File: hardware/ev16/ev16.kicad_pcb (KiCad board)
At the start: 4 copper layers, 109.8 x 80 mm, 162 parts, among them CN1 Conn_05x02_Female, CN2 PJ-242, J1 USB_C_Receptacle, J11 Conn_02x05_Counter_Clockwise, J2 Conn_01x02_Socket, J3 AudioJack4, J4 Conn_02x03_Odd_Even, J5 Conn_02x03_Odd_Even, J6 Conn_02x05_Counter_Clockwise, J7 Conn_02x05_Counter_Clockwise, J8 Conn_02x05_Counter_Clockwise, J9 Conn_02x05_Counter_Clockwise, Q1 2N7002, SW1 SW_SPDT, SW2 SW_Push, SW3 SW_Push, SW4 SW_Push, SW5 SW_Push, SW6 SW_Push, SW7 SW_Push, U1 BQ21040DBV, U10 STM32F405RGTx, U2 USBLC6-2P6, U3 STM32F072CBTx, U4 CH340C, U5 TPS63060, U6 WM8960CGEFL/RV, U7 ESP32-S3-WROOM-1, U8 M24C02-RMN6TP, Y1 Crystal_GND24

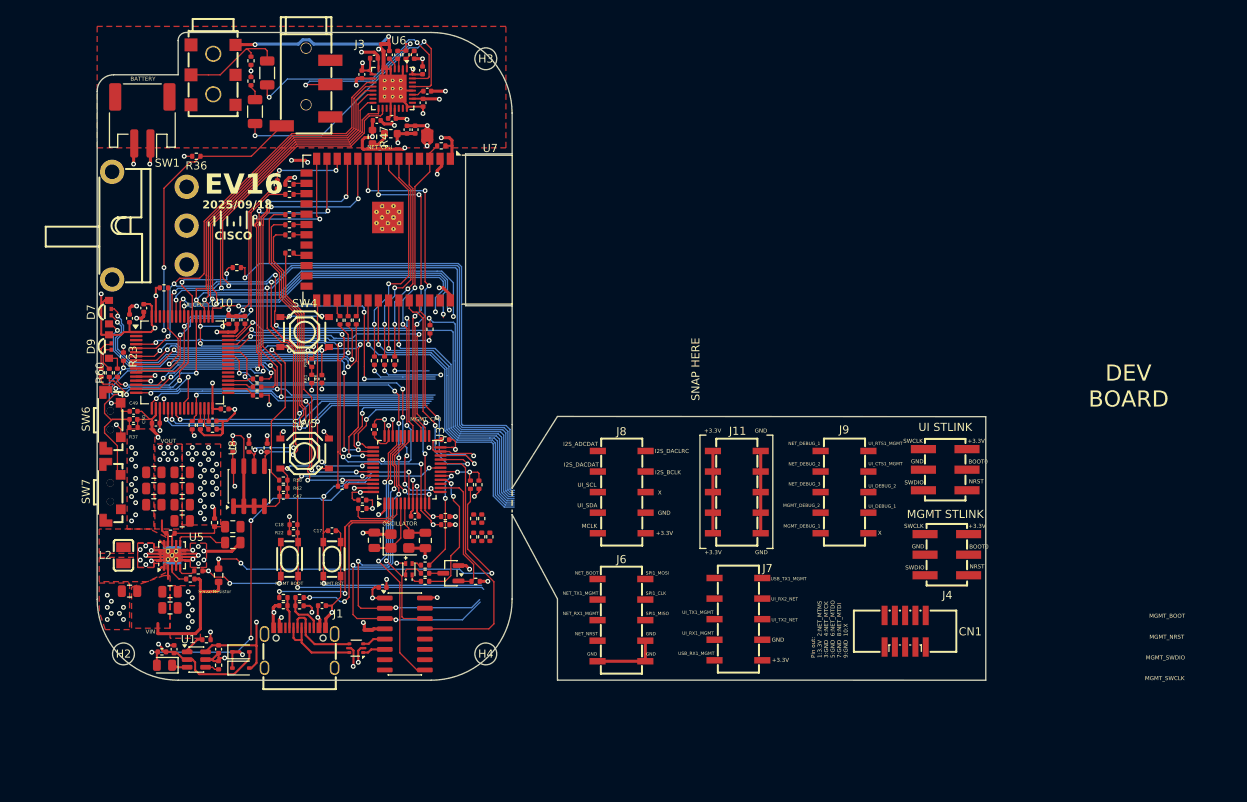
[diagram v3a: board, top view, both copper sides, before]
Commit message: finish wiring up the remaining connections between chips and dev board. Added charging detect wiring
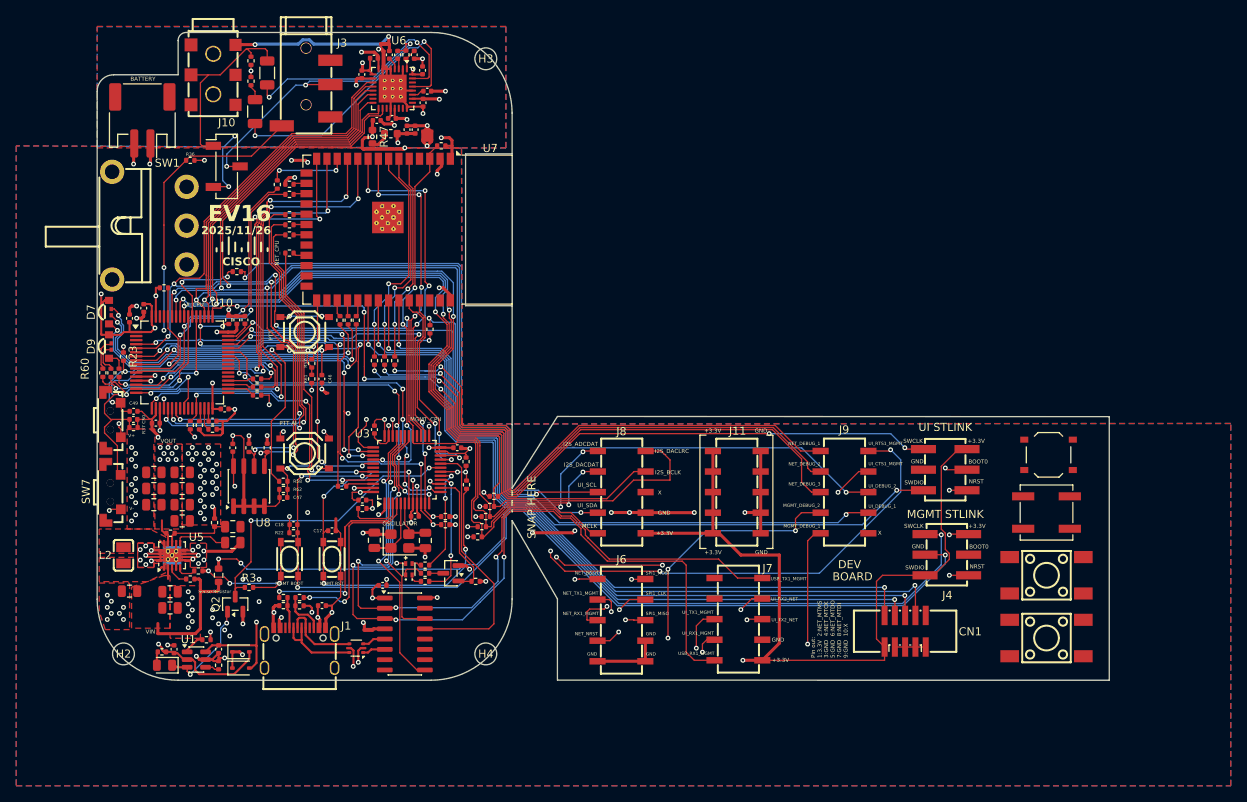
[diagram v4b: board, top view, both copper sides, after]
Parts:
- added J10: Conn_01x03_Pin, Connector_PinSocket_2.54mm:PinSocket_1x03_P2.54mm_Vertical_SMD_Pin1Left, F.Cu at (66.0, 46.5)
- added Q2: 2N7002, Package_TO_SOT_SMD:SOT-23, F.Cu at (67.0, 100.6)
- added R3: 47k, Resistor_SMD:R_0402_1005Metric, F.Cu at (68.8, 98.5)
- added REF**: SW_Push_1P1T_XKB_TS-1187A, Button_Switch_SMD:SW_Push_1P1T_XKB_TS-1187A, F.Cu at (167.5, 82.2)
- added REF**: SW_SPST_B3SL-1022P, Button_Switch_SMD:SW_SPST_B3SL-1022P, F.Cu at (167.2, 89.3)
- added REF**: SW-SMD_4P-L6.0-W6.0-P4.50-LS9.0_H5.0, Hactar_Footprints:SW-SMD_4P-L6.0-W6.0-P4.5, F.Cu at (167.2, 97.0)
- added REF**: SW-SMD_4P-L6.0-W6.0-P4.50-LS9.0_H5.0, Hactar_Footprints:SW-SMD_4P-L6.0-W6.0-P4.5, F.Cu at (167.2, 104.8)
- moved R13 3.26 mm to (95.6, 83.0), turned to 90 degrees
- moved R69 3.13 mm to (99.0, 87.3), turned to 180 degrees
- moved R68 2.55 mm to (98.0, 89.8), turned to 180 degrees
- moved R67 2.50 mm to (98.5, 88.5), turned to 180 degrees
- moved C6 1.79 mm to (94.5, 81.3), turned to 180 degrees
- moved R66 1.25 mm to (97.5, 91.0), turned to 180 degrees
- moved R36 0.90 mm to (61.5, 45.8), turned to 0 degrees
- moved R64 0.50 mm to (97.0, 92.3), turned to 180 degrees
- moved R73 0.50 mm to (67.2, 59.5)
- moved R12 0.48 mm to (95.6, 85.9)
- moved C13 0.25 mm to (85.2, 98.3)
- moved R41 0.24 mm to (61.5, 78.5)
- moved R56 0.20 mm to (50.7, 72.0)
- moved R59 0.20 mm to (52.7, 72.0)
- moved R60 0.20 mm to (51.7, 72.0)
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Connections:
- D1 pad 2: /CHG_FB -> Net-(D1-A)
- R11 pad 2: /CHG_FB -> Net-(D1-A)
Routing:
- net +3.3V: track 169.3 -> 302.9 mm, vias 44 -> 45
- net /MGMT_SWDIO: track 2.06 -> 100.0 mm, vias 1 -> 2
- net /UI_BOOT0: track 60.1 -> 154.0 mm, vias 5 -> 6
- net /MGMT_SWCLK: track 11.0 -> 100.8 mm
- net /UI_NRST: track 47.0 -> 130.3 mm, vias 4 -> 5
- net GND: track 236.5 -> 315.4 mm, vias 104 -> 126
- net /MGMT_DEBUG_2: track 0.00 -> 77.9 mm, vias 0 -> 4
- net /MGMT_DEBUG_1: track 0.00 -> 76.4 mm, vias 0 -> 2
- net /UI_SWCLK: track 37.5 -> 113.8 mm, vias 3 -> 6
- net /UI_RTS1_MGMT: track 49.8 -> 125.8 mm, vias 5 -> 8
- net /MGMT_NRST: track 46.7 -> 121.6 mm, vias 3 -> 4
- net /MGMT_BOOT: track 46.0 -> 119.0 mm, vias 3 -> 4
- net Net-(J9-Pin_8): track 8.56 -> 76.8 mm, vias 1 -> 2
- net Net-(J9-Pin_6): track 5.00 -> 72.7 mm, vias 1 -> 2
- net /UI_CTS1_MGMT: track 49.5 -> 115.7 mm, vias 5 -> 8
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- added copper zone on B.Cu, net GND
- added copper zone on B.Cu, net GNDA
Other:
- board size 109.8 x 80 mm -> 125 x 80 mm
- board text added: "2025/11/26"
- board text added: "PTT"
- board text added: "PTT AI"
- board text added: "V+"
- board text added: "V-"
- board text removed: "2025/09/18"
- board text removed: "MGMT_BOOT"
- board text removed: "MGMT_NRST"
- board text removed: "MGMT_SWCLK"
- board text removed: "MGMT_SWDIO"

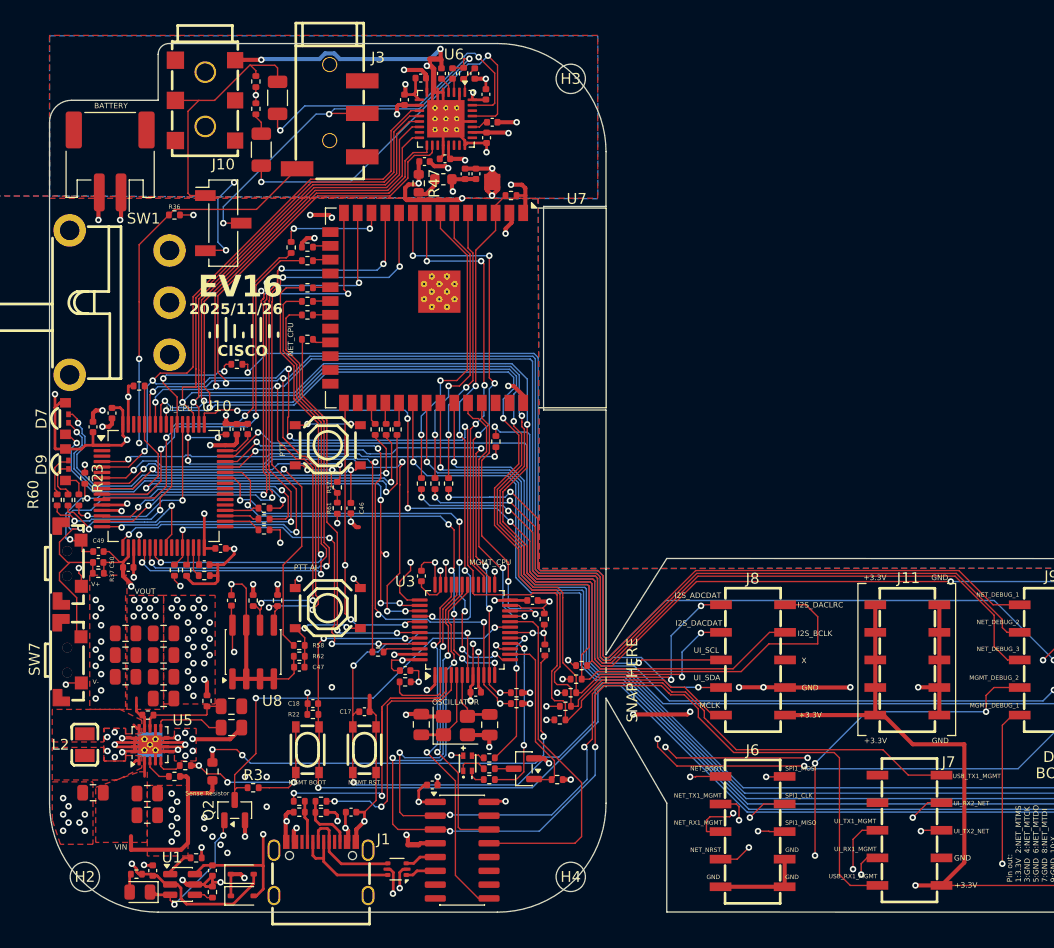
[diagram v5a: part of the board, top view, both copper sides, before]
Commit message: stitched ground planes with vias, changed pins for volume up and down
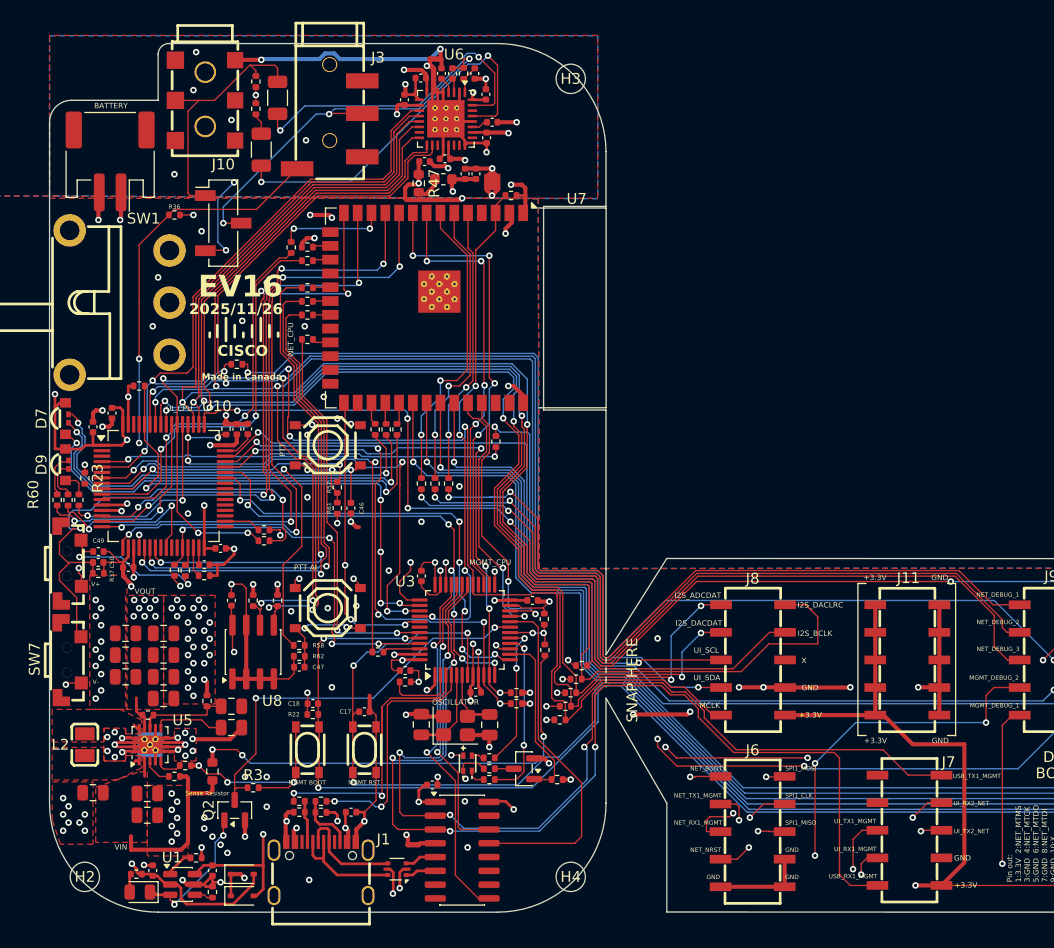
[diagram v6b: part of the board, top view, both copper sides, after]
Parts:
- removed R40: 4k7, Resistor_SMD:R_0402_1005Metric
- moved R17 8.67 mm to (62.5, 78.5), turned to -90 degrees
- moved R24 3.00 mm to (69.8, 75.8)
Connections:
- R73 pad 2: /UI_DEBUG_2 -> /VOLUME-
- U10 pad 29: Net-(U10-PB10) -> /VOLUME+
- U10 pad 35: /VOLUME+ -> unconnected-(U10-PB14-Pad35)
- U10 pad 36: /VOLUME- -> unconnected-(U10-PB15-Pad36)
- U10 pad 54: /UI_DEBUG_2 -> /VOLUME-
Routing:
- net /VOLUME-: track 3.15 -> 28.7 mm, vias 0 -> 4
- net Net-(C49-Pad1): track 32.9 -> 14.6 mm, vias 3 -> 2
- net /UI_DEBUG_2: track 11.9 -> 0.00 mm, vias 2 -> 0
- net GND: track 315.4 -> 309.9 mm, vias 126 -> 147
- net Net-(C50-Pad1): track 41.3 -> 44.7 mm
- net +3.3V: track 302.9 -> 306.0 mm
- net Net-(U10-PB10): track 1.63 -> 0.00 mm
- net /VOLUME+: track 3.19 -> 1.84 mm
- net /USB_TX1_MGMT: track 89.9 -> 90.9 mm
- net /MGMT_DEBUG_2: track 77.9 -> 78.5 mm
- net GNDA: vias 8 -> 13
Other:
- board text added: "Made in Canada"
